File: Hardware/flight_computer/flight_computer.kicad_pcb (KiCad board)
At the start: 4 copper layers, 80 x 100 mm, 118 parts, among them J1 Micro_USB, J2 MicroSD_molex, J3 rpi_zero_w, J4 JST_8_RA, J5 JST_GH_6_RA, J6 JST_GH_4_RA, J7 JST_GH_5_RA, J8 Conn_02x03, J9 Conn_02x03, Q2 PMOS_20V_.76A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

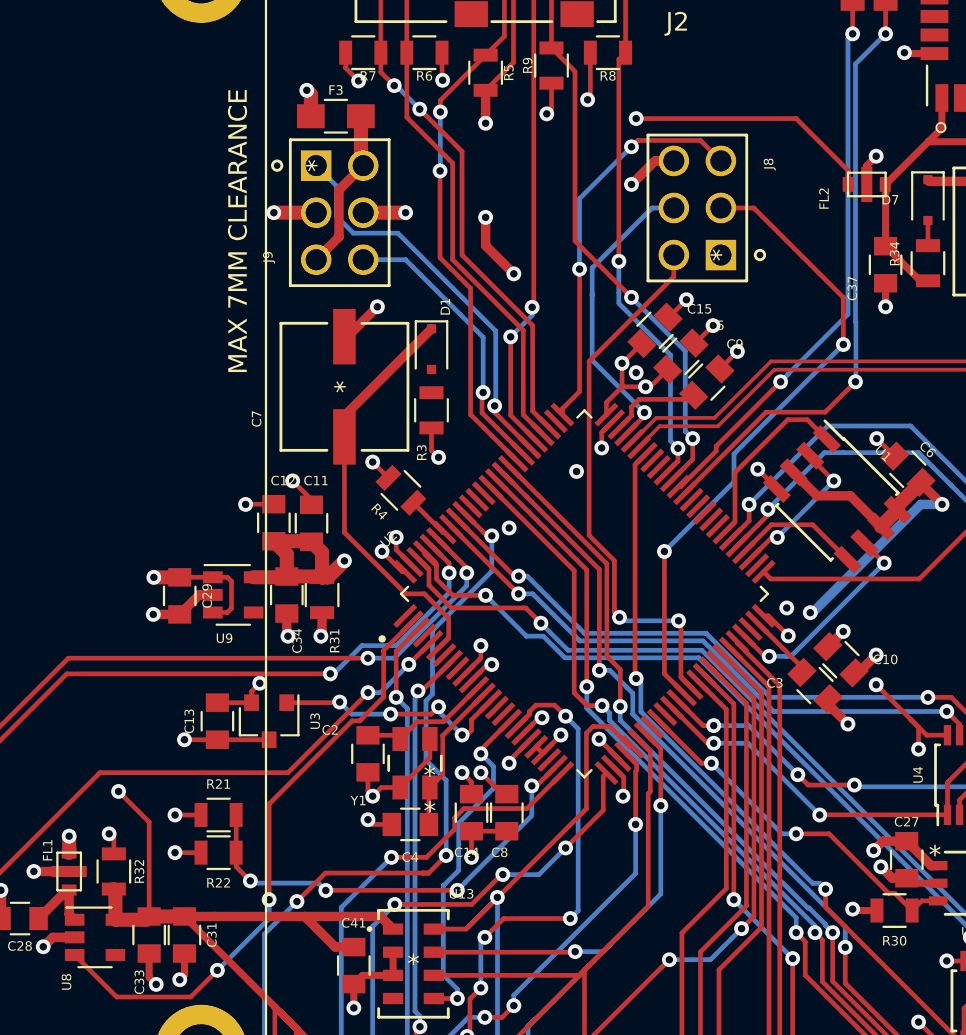
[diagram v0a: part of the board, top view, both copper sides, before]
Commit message: Thickens gps power trace and updates servo connector pins
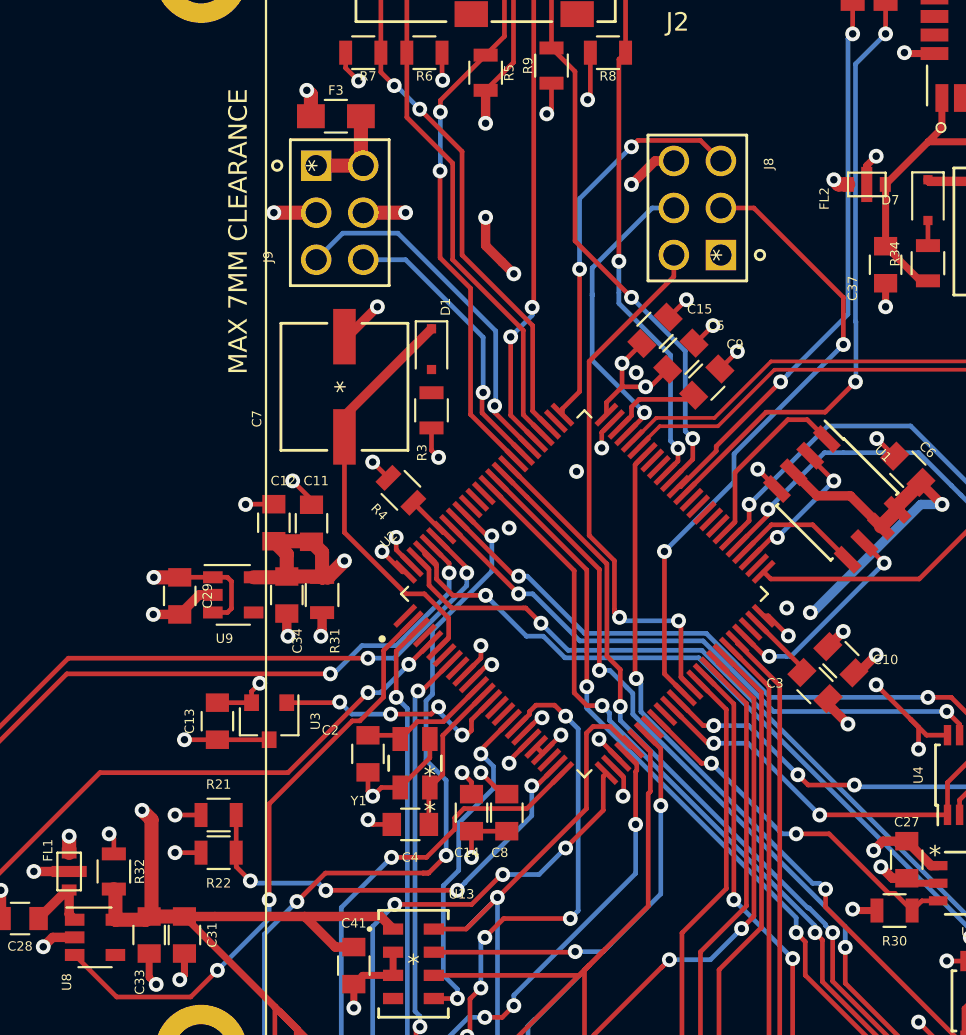
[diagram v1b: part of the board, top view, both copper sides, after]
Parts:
- removed G***: LOGO, drone_footprints:osprey_bitmap
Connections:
- J9 pad 1: /SERVO_CH1_GPIO -> /VDD_5V_AUX
- J9 pad 5: /VDD_5V_AUX -> /SERVO_CH1_GPIO
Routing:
- net /VDD_5V_AUX: track 8.85 -> 5.26 mm
- net /SERVO_CH1_GPIO: track 21.4 -> 19.6 mm
- net /VDD_3V3_SENSORS: track 143.8 -> 144.4 mm

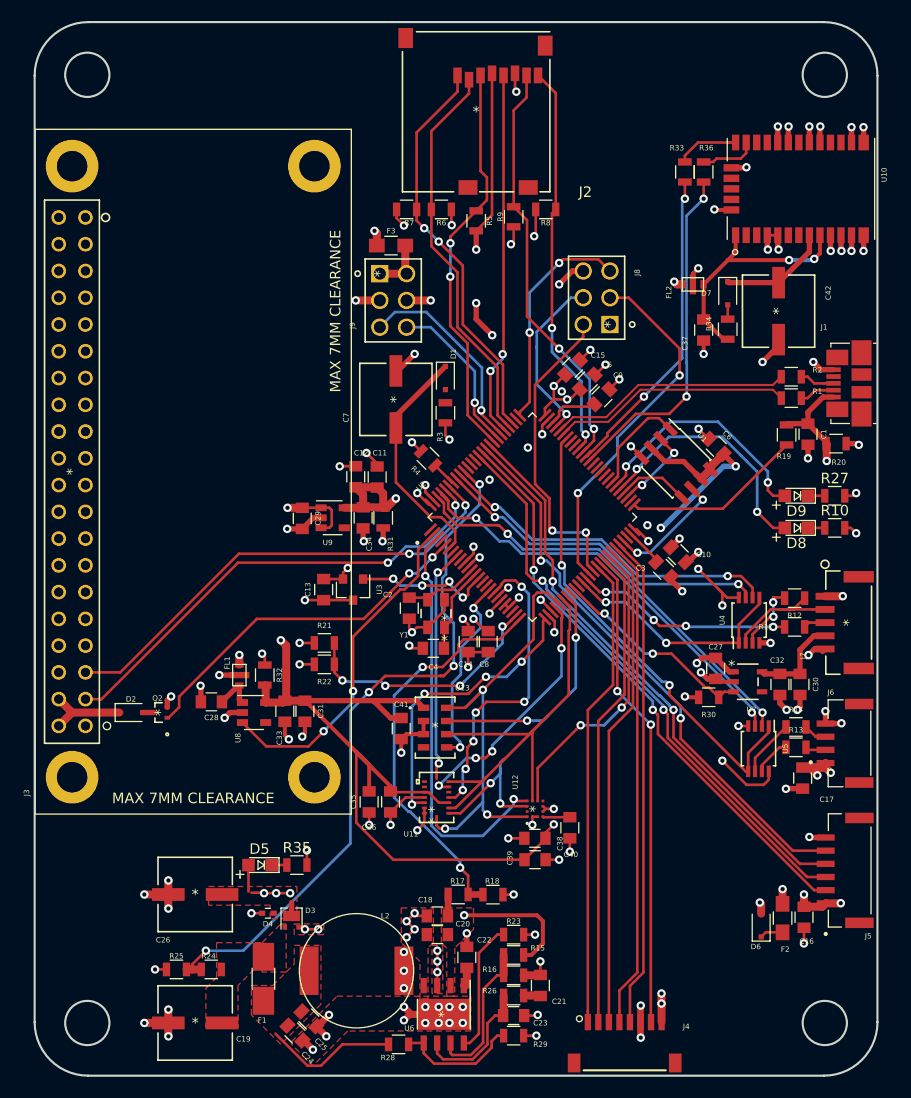
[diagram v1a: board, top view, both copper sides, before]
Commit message: added switch components, worked on layout. Sensor 3V3 unfinished.
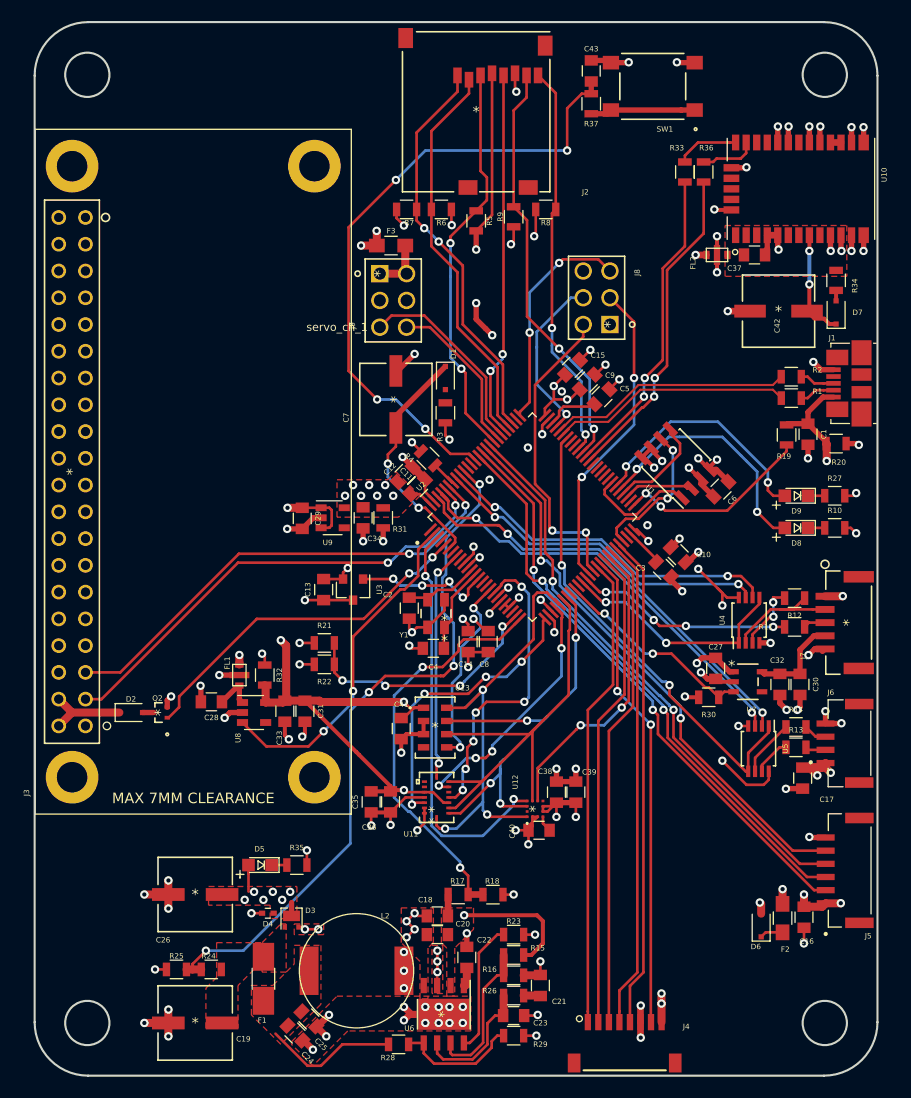
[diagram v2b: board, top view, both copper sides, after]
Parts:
- added C43: C_10u, Capacitors_SMD:C_0805, F.Cu at (132.3, 65.1)
- added R37: R_10K, Resistors_SMD:R_0805, F.Cu at (132.3, 68.2)
- added SW1: Switch_SMT, drone_footprints:PTS645SM43SMTR92LFS, F.Cu at (138.2, 66.5)
- moved R34 11.3 mm to (155.6, 85.0), turned to 90 degrees
- moved D7 10.4 mm to (155.6, 88.0), turned to 90 degrees
- moved C37 8.61 mm to (147.8, 82.5), turned to 180 degrees
- moved C39 7.49 mm to (130.9, 133.5), turned to 90 degrees
- moved C38 4.84 mm to (129.0, 133.5), turned to 90 degrees
- moved C12 4.70 mm to (114.7, 103.4), turned to 225 degrees
- moved C6 4.08 mm to (144.7, 104.8), turned to 225 degrees
- moved C11 3.94 mm to (115.8, 104.5), turned to 225 degrees
- moved FL2 3.61 mm to (144.3, 82.5)
- moved C40 2.93 mm to (127.4, 137.2), turned to 180 degrees
- moved C35 0.19 mm to (111.4, 134.5)
- turned C42 to 180 degrees
- turned U1 to 135 degrees
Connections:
- U2 pad 88: Net-(U2-Pad88) -> /SWITCH
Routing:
- net /SWITCH: track 0.00 -> 60.9 mm, vias 0 -> 4
- net /VDD_3V3_SENSORS: track 144.4 -> 119.3 mm, vias 4 -> 6
- net /VDD_3V3_STM: track 178.2 -> 155.0 mm, vias 30 -> 36
- net /Sensors/GPS_VCC: track 23.1 -> 0.00 mm, vias 2 -> 0
- net Net-(R37-Pad2): track 0.00 -> 9.96 mm
- net /VDD_5V_USB: track 79.1 -> 88.6 mm
- net GND: track 241.1 -> 248.8 mm, vias 109 -> 105
- net /FMU_UART7_RX: track 34.5 -> 29.8 mm
- net /FRAM_MOSI: track 6.99 -> 9.68 mm
- net /VDD_5V_IN: track 24.2 -> 21.9 mm, vias 10 -> 14
- net /FRAM_SCK: track 11.6 -> 13.9 mm
- net /GPS_USART6_TX: track 32.8 -> 30.9 mm
- net /FRAM_MISO: track 8.12 -> 6.66 mm, vias 2 -> 0
- net /VDD_USB_VALID: track 17.1 -> 18.5 mm, vias 0 -> 2
- net Net-(C40-Pad1): track 2.57 -> 1.54 mm
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- added copper zone on F.Cu, net /Sensors/GPS_VCC
- added copper zone on In2.Cu, net /VDD_3V3_SENSORS
- added copper zone on F.Cu, net /VDD_3V3_STM
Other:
- board text added: "servo_ch_1"

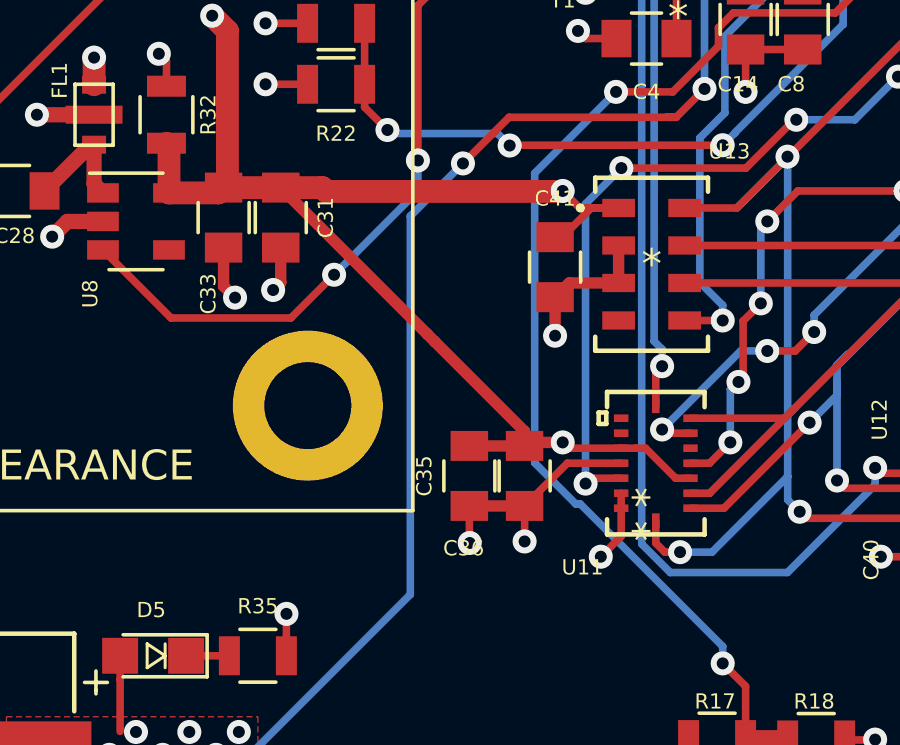
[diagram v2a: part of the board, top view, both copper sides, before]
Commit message: Moves sensor capacitors
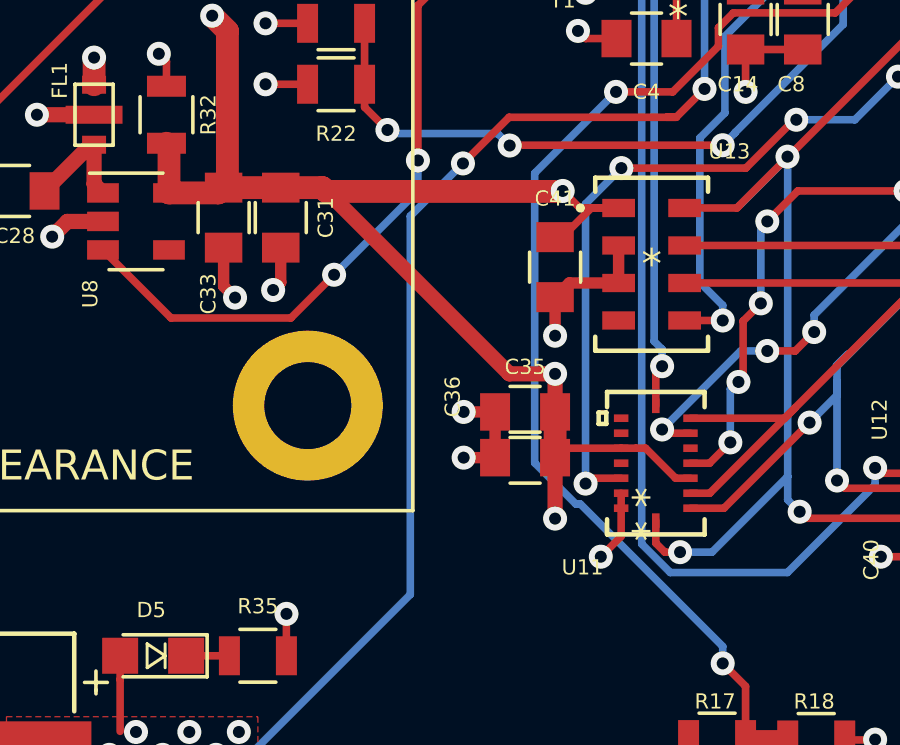
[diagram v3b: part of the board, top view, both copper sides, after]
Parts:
- moved C35 2.83 mm to (113.3, 132.3), turned to 0 degrees
- moved C36 0.61 mm to (113.3, 133.9), turned to 180 degrees
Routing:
- net GND: track 248.8 -> 244.4 mm
- net /VDD_3V3_SENSORS: track 119.3 -> 119.6 mm, vias 6 -> 7

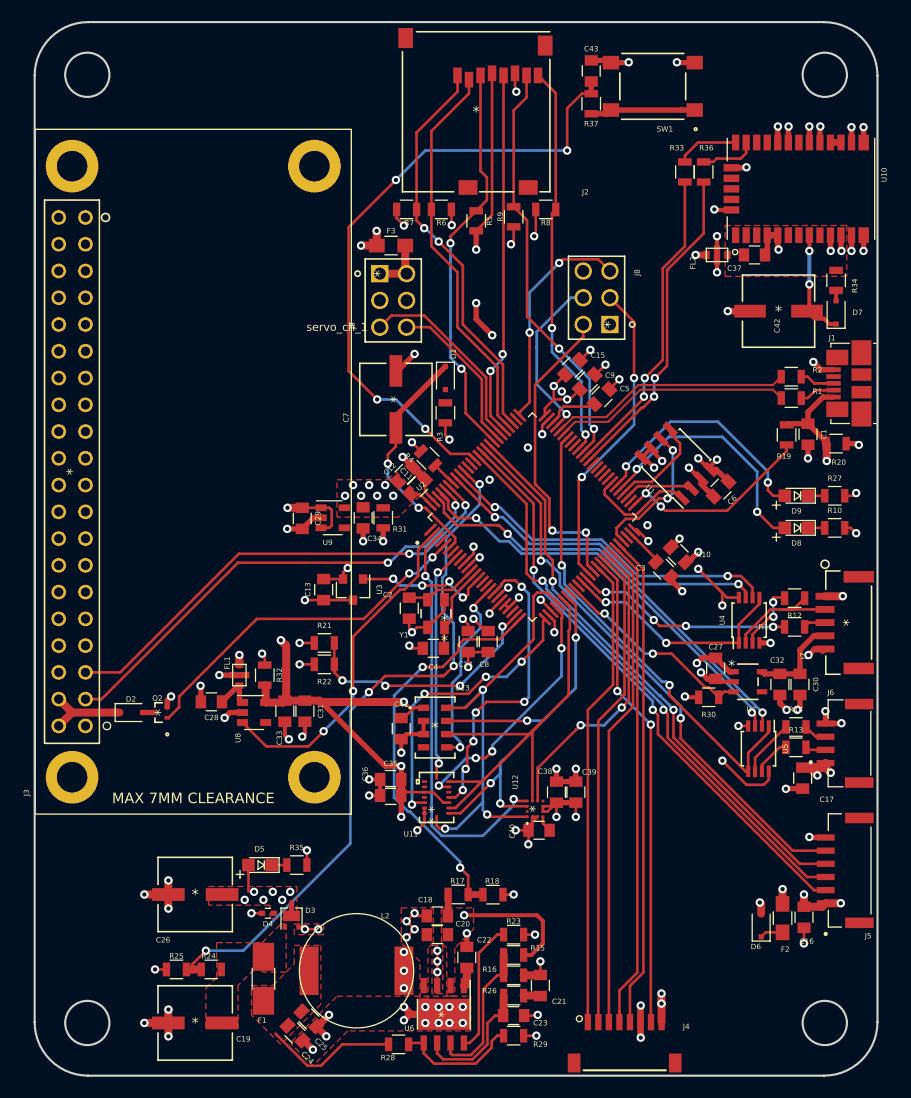
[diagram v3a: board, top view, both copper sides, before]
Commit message: Adds labels to silkscreen
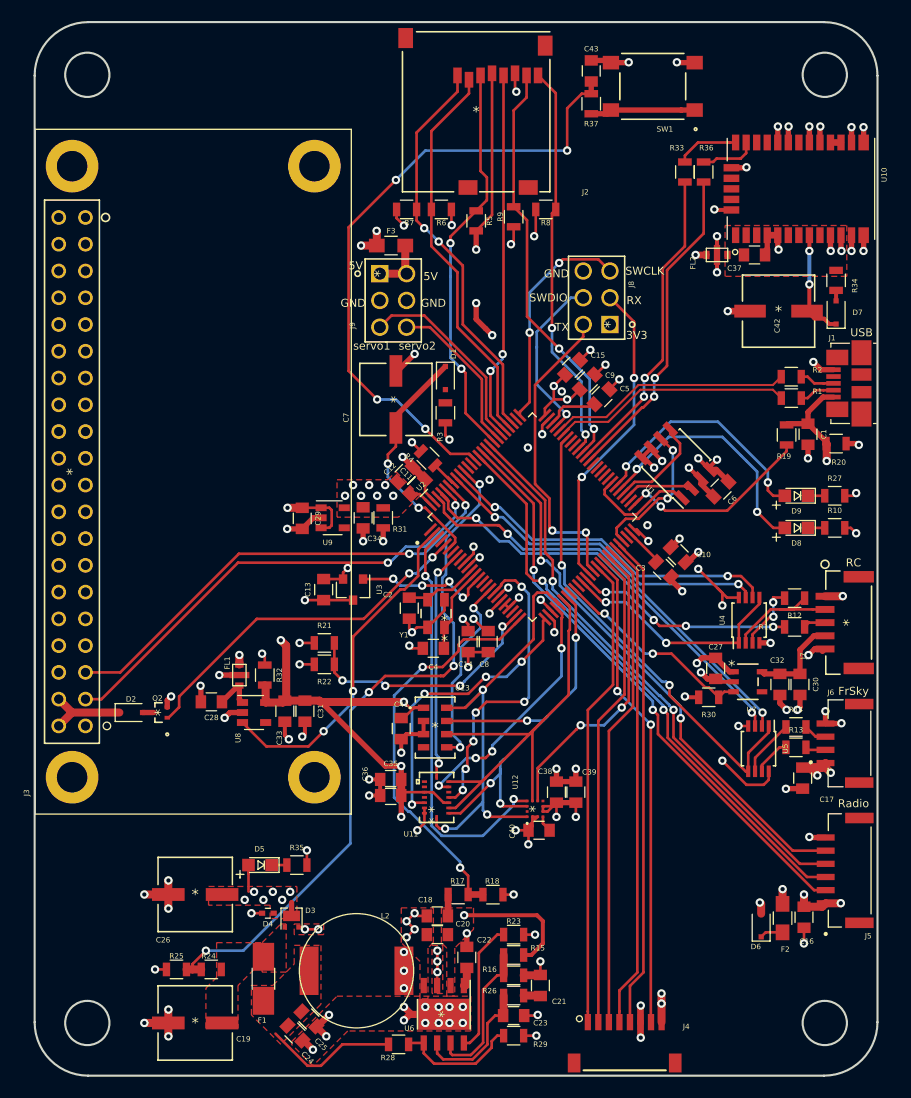
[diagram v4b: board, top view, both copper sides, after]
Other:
- board text added: "3V3"
- board text added: "5V"
- board text added: "FrSky"
- board text added: "GND"
- board text added: "RC"
- board text added: "RX"
- board text added: "Radio"
- board text added: "SWCLK"
- board text added: "SWDIO"
- board text added: "TX"
- board text added: "USB"
- board text added: "servo1"
- board text added: "servo2"
- board text removed: "servo_ch_1"
